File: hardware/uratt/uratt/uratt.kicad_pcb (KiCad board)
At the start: 2 copper layers, 50 x 62 mm, 139 parts, among them J1 USB_B_Micro, J10 Conn_01x10, J2 Micro_SD_Card, J3 Conn_01x10, J4 Conn_01x04, J5 Conn_01x04, J6 Conn_01x02, J7 Conn_01x02, J8 Conn_01x02, P1 TOUCH, Q1 MMBT3904, Q2 MMBT3904, Q3 2N7002, Q4 DMP31D0U, SW1 SW_Push, SW2 SW_Push, SW3 SW_Push (OPTION), U1 SN65220, U2 CP2102N-A01-GQFN24, U3 ESP32-WROOM-32, U4 MCP73832-2-OT, U5 TPS2115A, U6 TPS61032PWP, U7 AP2112K-3.3, U8 AP2112K-3.3, U9 MP6513

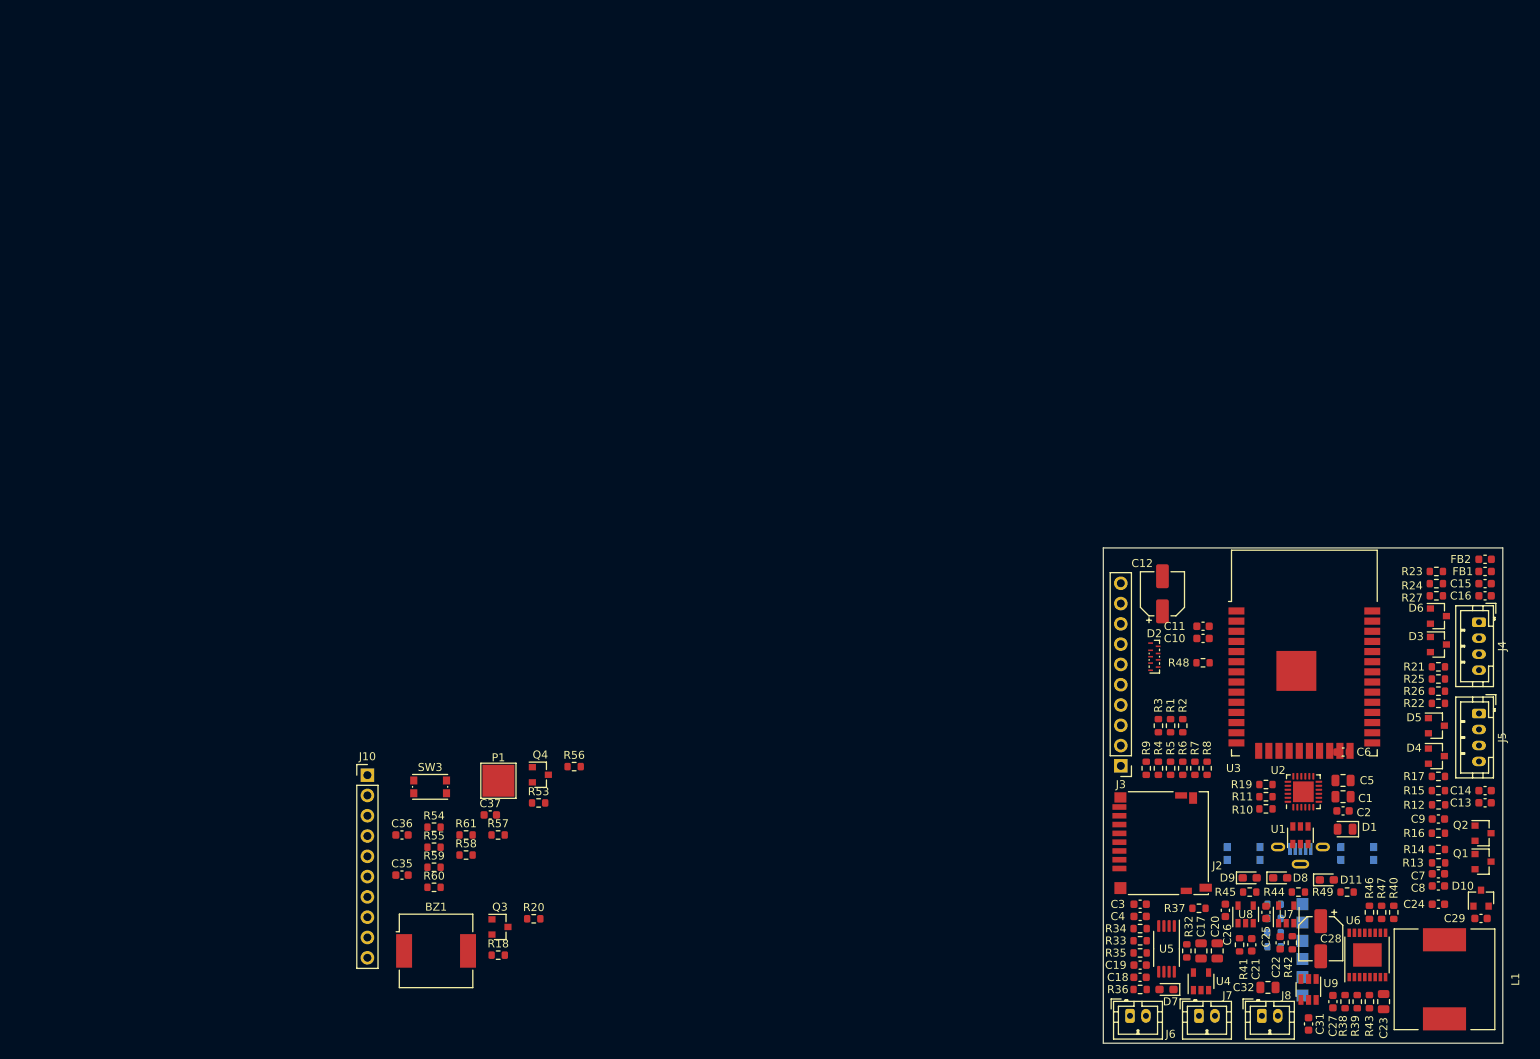
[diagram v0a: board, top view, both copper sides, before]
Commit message: import actual board outline DXF and adjust rough placement
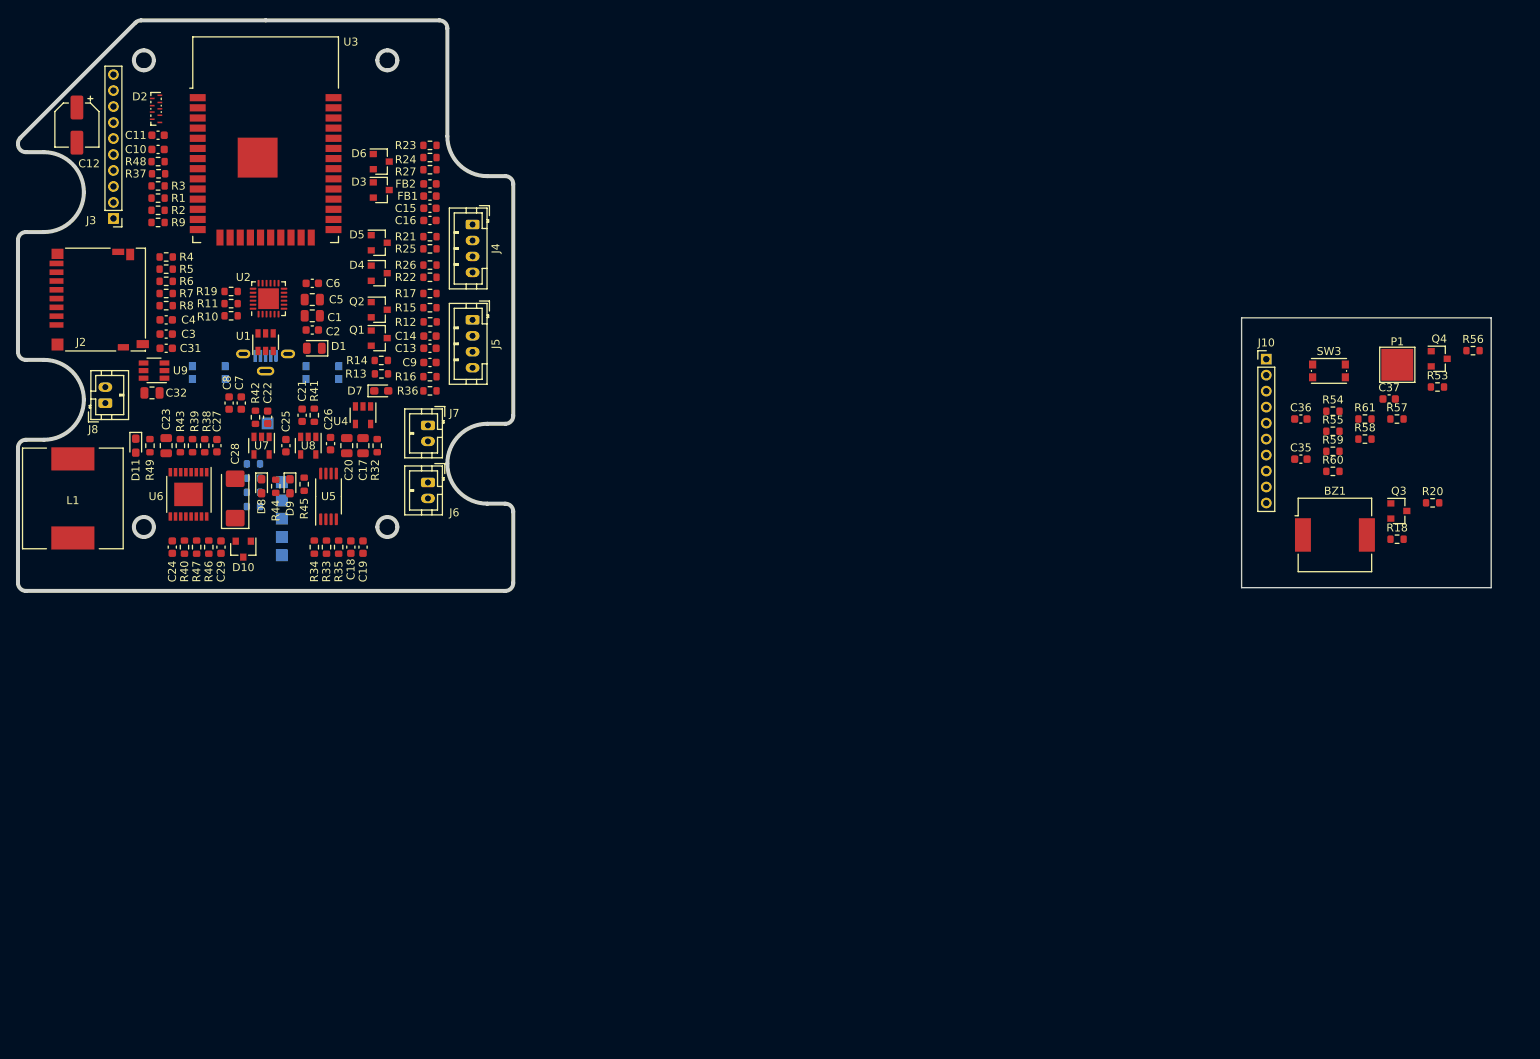
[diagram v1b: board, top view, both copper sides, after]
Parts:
- C28: footprint Capacitor_SMD:CP_Elec_5x3 -> Capacitor_Tantalum_SMD:CP_EIA-6032-20_AVX-F
- J10, J3: footprint Connector_PinHeader_2.54mm:PinHeader_1x10_P2.54mm_Vertical -> Connector_PinHeader_2.00mm:PinHeader_1x10_P2.00mm_Vertical
- moved L1 182.0 mm to (32.0, 82.8), turned to 90 degrees
- moved C23 167.5 mm to (43.7, 76.2), turned to 270 degrees
- moved C31 166.1 mm to (43.7, 64.0), turned to 0 degrees
- moved C24 164.7 mm to (44.5, 88.9), turned to 90 degrees
- moved C29 164.4 mm to (50.5, 88.9), turned to 90 degrees
- moved R43 164.3 mm to (45.5, 76.2), turned to 270 degrees
- moved U9 164.0 mm to (42.2, 66.8), turned to 180 degrees
- moved J8 163.8 mm to (36.1, 70.9), turned to 90 degrees
- moved C8 163.0 mm to (51.6, 70.9), turned to 270 degrees
- moved R39 161.6 mm to (47.0, 76.2), turned to 90 degrees
- moved C7 161.0 mm to (53.1, 70.9), turned to 270 degrees
- moved D10 161.0 mm to (53.3, 89.2), turned to 270 degrees
- moved R49 159.9 mm to (41.7, 76.2), turned to 90 degrees
- moved R37 159.4 mm to (42.7, 42.2), turned to 180 degrees
- moved R38 158.8 mm to (48.5, 76.2), turned to 270 degrees
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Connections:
- Q3 pad 2: GND -> GND1
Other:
- board size 50 x 62 mm -> 184.4 x 71.4 mm

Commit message: WIP routing
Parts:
- removed the C32 at (41.9, 69.6)
- removed the R41 at (62.2, 72.4)
- removed the R42 at (54.9, 72.6)
- removed the R44 at (57.4, 81.3)
- removed the R45 at (61.0, 81.0)
- added C30: 0.1uF, Capacitor_SMD:C_0603_1608Metric, F.Cu at (47.5, 67.6)
- added H1: MountingHole, MountingHole:MountingHole_2.7mm_M2.5, F.Cu at (40.9, 27.8)
- added H2: MountingHole, MountingHole:MountingHole_2.7mm_M2.5, F.Cu at (71.4, 27.8)
- added H3: MountingHole, MountingHole:MountingHole_2.7mm_M2.5, F.Cu at (40.9, 86.2)
- added H4: MountingHole, MountingHole:MountingHole_2.7mm_M2.5, F.Cu at (71.4, 86.2)
- added H5: MountingHole, MountingHole:MountingHole_2.7mm_M2.5, F.Cu at (30.5, 101.6)
- added H6: MountingHole, MountingHole:MountingHole_2.7mm_M2.5, F.Cu at (94.5, 97.0)
- added H7: MountingHole, MountingHole:MountingHole_2.7mm_M2.5, F.Cu at (29.5, 116.8)
- added H8: MountingHole, MountingHole:MountingHole_2.7mm_M2.5, F.Cu at (94.5, 112.8)
- added LCD1: ER-TFT0.96-1, uratt:ER-TFT0.96-1, B.Cu at (42.1, 114.1)
- added R35: 1K, Resistor_SMD:R_0603_1608Metric, F.Cu at (61.5, 74.4)
- added R36: 1K, Resistor_SMD:R_0603_1608Metric, F.Cu at (54.1, 74.7)
- added R37: 1K, Resistor_SMD:R_0603_1608Metric, F.Cu at (55.4, 82.8)
- added R38: 1K, Resistor_SMD:R_0603_1608Metric, F.Cu at (58.9, 82.8)
- BZ1: moved to B.Cu
- C31: value 0.1uF -> 10uF; footprint Capacitor_SMD:C_0603_1608Metric -> Capacitor_SMD:C_0805_2012Metric
- C32: renamed from C35; moved to B.Cu
- C33: renamed from C36; moved to B.Cu
- C34: renamed from C37; moved to B.Cu
- GT1: renamed from R43; footprint Resistor_SMD:R_0603_1608Metric -> uratt:GND_TIE
- J1: footprint Connector_USB:USB_Micro-B_Molex-105133-0001 -> Connector_FFC-FPC:TE_1-1734839-0_1x10-1MP_P0.5mm_Horizontal
- J3: footprint Connector_PinHeader_2.00mm:PinHeader_1x10_P2.00mm_Vertical -> Connector_FFC-FPC:Hirose_FH12-10S-0.5SH_1x10-1MP_P0.50mm_Horizontal
- J9: renamed from J10; footprint Connector_PinHeader_2.00mm:PinHeader_1x10_P2.00mm_Vertical -> Connector_FFC-FPC:TE_1-1734839-0_1x10-1MP_P0.5mm_Horizontal; moved to B.Cu
- JP1: renamed from R28; moved to F.Cu
- JP2: renamed from R29; moved to F.Cu
- JP3: renamed from R30; moved to F.Cu
- JP4: renamed from R31; moved to F.Cu
- Q3: renamed from Q4; moved to B.Cu
- Q4: renamed from Q3; moved to B.Cu
- R43: renamed from R53; moved to B.Cu
- R44: renamed from R54; moved to B.Cu
- R45: renamed from R55; moved to B.Cu
- R46: renamed from R56; moved to B.Cu
- R47: renamed from R57; moved to B.Cu
- R48: renamed from R58; moved to B.Cu
- R49: renamed from R59; moved to B.Cu
- R50: renamed from R60; moved to B.Cu
- R51: renamed from R61; moved to B.Cu
- R52: renamed from R18; moved to B.Cu
- R53: renamed from R20; moved to B.Cu
- TP1, TP2, TP3, TP4, TP5, TP6: footprint TestPoint:TestPoint_Pad_1.5x1.5mm -> TestPoint:TestPoint_Pad_D1.0mm
- U6: footprint Package_SO:TSSOP-16-1EP_4.4x5mm_P0.65mm -> uratt:PWP0016C
- moved R46 155.4 mm to (58.4, 109.0)
- moved Q3 149.7 mm to (61.7, 114.6)
- moved C34 149.6 mm to (54.6, 116.8)
- moved R53 146.3 mm to (58.4, 110.5)
- moved R47 142.9 mm to (58.4, 104.4)
- moved R51 140.9 mm to (58.4, 112.0), turned to 180 degrees
- moved R48 139.1 mm to (58.4, 107.4)
- moved R43 138.6 mm to (72.9, 117.1)
- moved C33 137.8 mm to (54.6, 115.3)
- moved R45 137.5 mm to (58.4, 115.3)
- moved R49 134.5 mm to (58.4, 105.9)
- moved R50 133.4 mm to (58.4, 102.9)
- moved R52 133.0 mm to (65.3, 99.3), turned to 180 degrees
- moved R44 132.1 mm to (65.0, 115.3)
- moved Q4 129.7 mm to (69.1, 98.3)
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- renumbered R19 to R18, R21 to R19, R22 to R20, R23 to R21, R24 to R22, R25 to R23, R26 to R24, R27 to R25, R32 to R26, R33 to R27, R34 to R28, R35 to R29, R36 to R30, R37 to R31, R38 to R32, R39 to R33, R40 to R34, R46 to R39, R47 to R40, R48 to R41, R49 to R42
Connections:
- C5 pad 1: +3V3 -> +3.3VSW
- C6 pad 1: +3V3 -> +3.3VSW
- D2 pad 2: LCD_CS -> LCD_RESET
- D2 pad 4: LCD_RESET -> LCD_MOSI
- D2 pad 5: LCD_DC -> FP_TOUCH_BTN
- D2 pad 6: LCD_CLK -> BEEPER
- D2 pad 7: LCD_MOSI -> LCD_CLK
- D2 pad 8: FP_TOUCH_BTN -> LCD_DC
- D2 pad 9: BEEPER -> LCD_CS
- U2 pad 5: +3V3 -> +3.3VSW
- U2 pad 6: +3V3 -> +3.3VSW
- U2 pad 7: +3V3 -> +3.3VSW
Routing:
- net +3.3VSW: track 0.00 -> 128.4 mm, vias 0 -> 19
- net PWR_ENABLE: track 0.00 -> 120.8 mm, vias 0 -> 6
- net +5VSW: track 0.00 -> 110.6 mm, vias 0 -> 14
- net GND: track 0.00 -> 89.3 mm, vias 0 -> 97
- net N_PWR_LOSS: track 0.00 -> 80.6 mm, vias 0 -> 4
- net LOW_BAT: track 0.00 -> 75.0 mm, vias 0 -> 2
- net SHUTDOWN: track 0.00 -> 71.0 mm, vias 0 -> 6
- net EN: track 0.00 -> 59.9 mm, vias 0 -> 4
- net +VSW: track 0.00 -> 53.4 mm, vias 0 -> 12
- net +5VUSB: track 0.00 -> 45.4 mm, vias 0 -> 6
- net RXD0: track 0.00 -> 37.7 mm, vias 0 -> 2
- net LCD_CS: track 0.00 -> 36.2 mm, vias 0 -> 2
- net TXD0: track 0.00 -> 35.0 mm, vias 0 -> 2
- net BEEPER: track 0.00 -> 34.1 mm, vias 0 -> 4
- net +5VIN: track 0.00 -> 28.9 mm, vias 0 -> 7
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- added copper zone on In1.Cu, net +3.3VSW
- added copper zone on In1.Cu, net +3V3
- added copper zone on In1.Cu, net +5VIN
- added copper zone on In1.Cu, net +5VSW
- added copper zone on In1.Cu, net +VSW
- added copper zone on In2.Cu, net GND
- added copper zone on In2.Cu, net GNDPWR
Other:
- board size 184.4 x 71.4 mm -> 62 x 96.6 mm
- copper layers 2 -> 4
- net class Default: clearance 0.2 -> 0.18; trace_width 0.25 -> 0.2; via_dia 0.8 -> 0.5; via_drill 0.4 -> 0.35
- net class Power added: clearance 0.2, trace_width 0.4, via_dia 0.5, via_drill 0.35
- rule trace_clearance: 0.2 -> 0.18

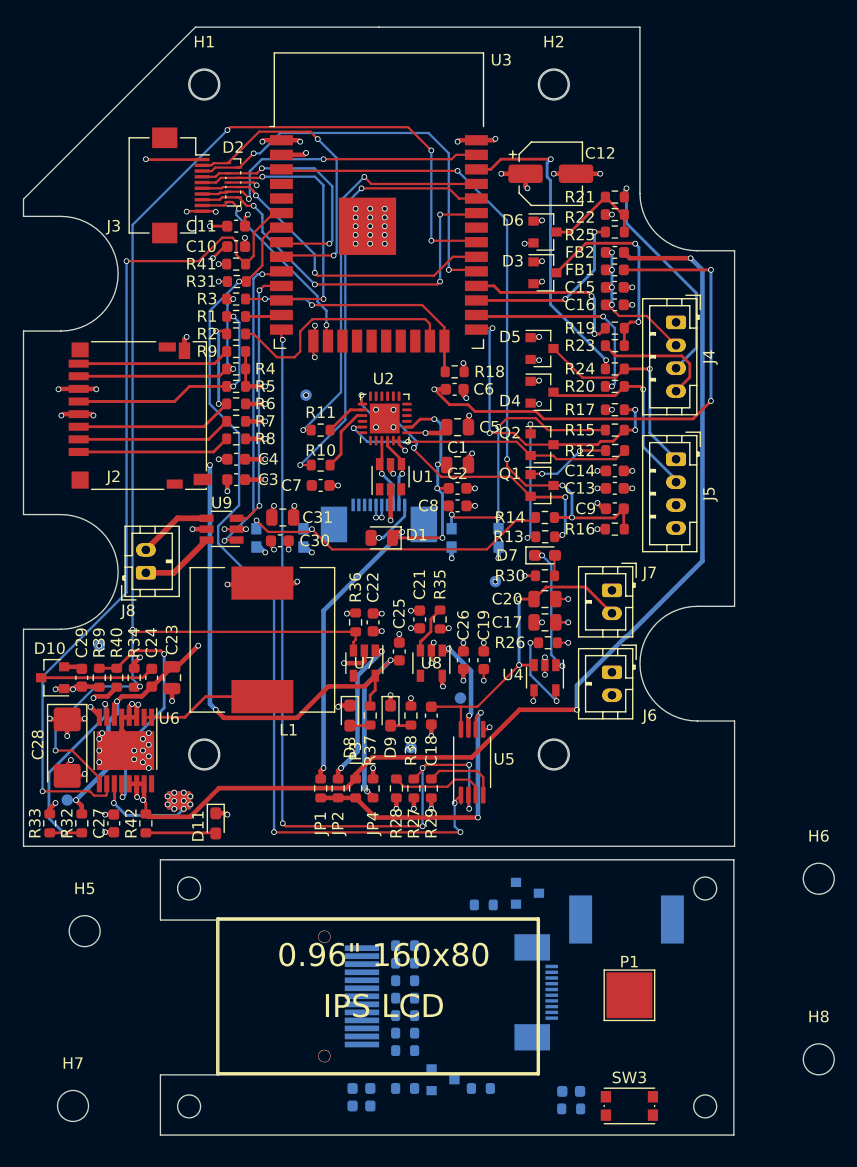
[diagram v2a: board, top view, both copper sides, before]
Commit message: fully routed, DRC'd, outlined w/breakaways, pending final review
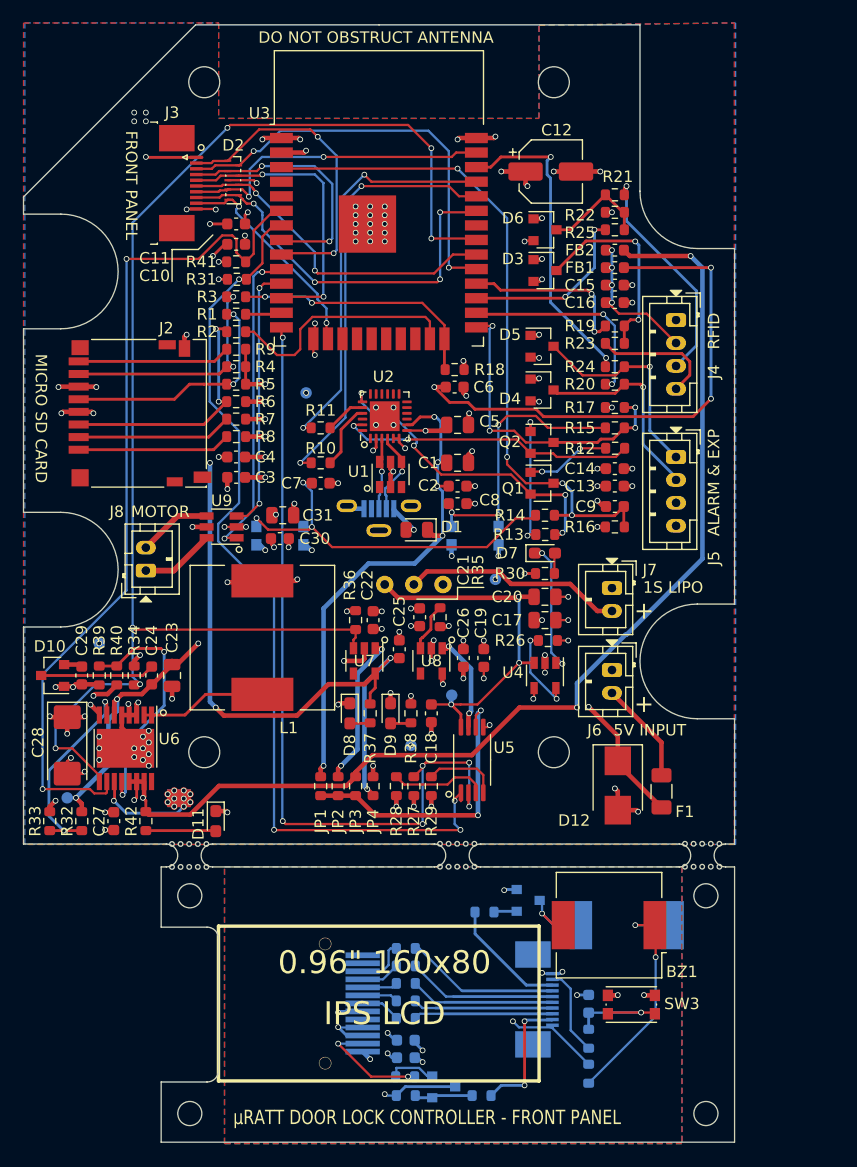
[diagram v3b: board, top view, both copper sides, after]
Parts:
- removed P1: TOUCH, TestPoint:TestPoint_Pad_4.0x4.0mm
- added BK1: BREAKAWAY, uratt:RATT_BITE, F.Cu at (37.6, 94.0)
- added BK2: BREAKAWAY, uratt:RATT_BITE, F.Cu at (61.0, 94.0)
- added BK3: BREAKAWAY, uratt:RATT_BITE, F.Cu at (82.3, 94.0)
- added BZ2: Buzzer (ALT OPT), Buzzer_Beeper:Buzzer_CUI_CPT-9019S-SMT, B.Cu at (77.7, 101.1)
- added D12: SM6T6V8A, Diode_SMD:D_SMB, F.Cu at (77.0, 88.9)
- added F1: MF-NSHT075KX-2, Fuse:Fuse_1206_3216Metric, F.Cu at (80.8, 89.4)
- added SW4: SW_SPDT, uratt:EAO-SPDT, B.Cu at (59.2, 71.4)
- BZ1: moved to F.Cu
- C32: value .1uF (OPTION) -> .1uF
- H5, H6, H7, H8: footprint MountingHole:MountingHole_2.7mm_M2.5 -> MountingHole:MountingHole_2.1mm
- J1: footprint Connector_FFC-FPC:TE_1-1734839-0_1x10-1MP_P0.5mm_Horizontal -> Connector_USB:USB_Micro-B_Molex-105133-0001
- J3: footprint Connector_FFC-FPC:Hirose_FH12-10S-0.5SH_1x10-1MP_P0.50mm_Horizontal -> Connector_FFC-FPC:TE_1-1734839-0_1x10-1MP_P0.5mm_Horizontal
- R43: value 470 (OPTION) -> 47
- SW3: value SW_Push (OPTION) -> SW_Push
- moved R53 16.4 mm to (74.4, 114.0), turned to 270 degrees
- moved H8 10.9 mm to (84.6, 117.5)
- moved H7 10.2 mm to (39.6, 117.5)
- moved H6 9.95 mm to (84.6, 98.5)
- moved H5 9.67 mm to (39.6, 98.5)
- moved SW3 8.84 mm to (78.1, 108.0)
- moved C32 7.79 mm to (74.4, 107.9), turned to 90 degrees
- moved R43 6.30 mm to (74.4, 111.0), turned to 90 degrees
- moved C33 5.72 mm to (58.5, 111.1)
- moved C34 5.72 mm to (58.5, 112.6)
- moved D1 3.13 mm to (59.4, 66.6)
- moved R51 2.27 mm to (58.4, 114.3), turned to 0 degrees
- moved R48 1.76 mm to (58.5, 109.2)
- moved BZ1 1.60 mm to (76.2, 101.1)
- moved R46 1.29 mm to (58.5, 107.7)
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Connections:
- J6 pad 2: +5VIN -> Net-(F1-Pad2)
- J7 pad 2: +VBATT -> Net-(J7-Pad2)
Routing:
- net /Front Panel/R_LCD_3.3V: track 0.00 -> 21.6 mm, vias 0 -> 5
- net Net-(BZ1-Pad1): track 0.00 -> 21.2 mm, vias 0 -> 2
- net Net-(J7-Pad2): track 0.00 -> 19.2 mm
- net /Front Panel/R_LCD_MOSI: track 0.00 -> 13.5 mm
- net /Front Panel/R_LCD_CLK: track 0.00 -> 13.1 mm
- net /Front Panel/R_LCD_DC: track 0.00 -> 12.6 mm
- net /Front Panel/R_LCD_RESET: track 0.00 -> 12.2 mm
- net /Front Panel/R_LCD_CS: track 0.00 -> 12.1 mm
- net +5VIN: track 28.9 -> 40.3 mm, vias 7 -> 8
- net /Front Panel/R_LCD_BL: track 0.00 -> 11.4 mm, vias 0 -> 2
- net GND1: track 0.00 -> 11.0 mm, vias 0 -> 10
- net /Front Panel/R_BEEPER: track 0.00 -> 10.5 mm
- net Net-(C32-Pad1): track 0.00 -> 10.2 mm, vias 0 -> 1
- net Net-(LCD1-Pad12): track 0.00 -> 10.0 mm, vias 0 -> 2
- net Net-(F1-Pad2): track 0.00 -> 8.97 mm
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- added copper zone on In1.Cu, net /Front Panel/R_LCD_3.3V
- added copper zone on B.Cu, net GND
- added copper zone on F.Cu, net GND
- added copper zone on B.Cu, net GND1
- added copper zone on F.Cu, net GND1
- added copper zone on In2.Cu, net GND1
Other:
- board size 62 x 96.6 mm -> 62 x 97.4 mm
- board text added: "+"
- board text added: "+3.3V"
- board text added: "+3.3VSW"
- board text added: "+5VIN"
- board text added: "+5VSW"
- board text added: "+VBATT"
- board text added: "+VSW"
- board text added: "1S LIPO"
- board text added: "5V INPUT"
- board text added: "ALARM & EXP"
- board text added: "BATT DISCON"
- board text added: "BOOT"
- board text added: "DESIGNED BY STEVE RICHARDSON"
- board text added: "DO NOT OBSTRUCT ANTENNA"
- board text added: "FRONT PANEL"
- board text added: "MICRO SD CARD"
- board text added: "MOTOR"
- board text added: "RESET"
- board text added: "REV 0 / 2020-DEC-21"
- board text added: "REV 0 / 2020-DEC-21 FIAT LUX"
- board text added: "RFID"
- board text added: "USB DEBUG"
- board text added: "www.makeitlabs.com"
- board text added: "µRATT DOOR LOCK CONTROLLER - FRONT PANEL"
- board text added: "µRATT ESP32 DOOR LOCK CONTROLLER"
